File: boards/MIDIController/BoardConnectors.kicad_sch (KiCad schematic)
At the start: 5 parts, among them J2 MIDICon, J3 IO_Boards

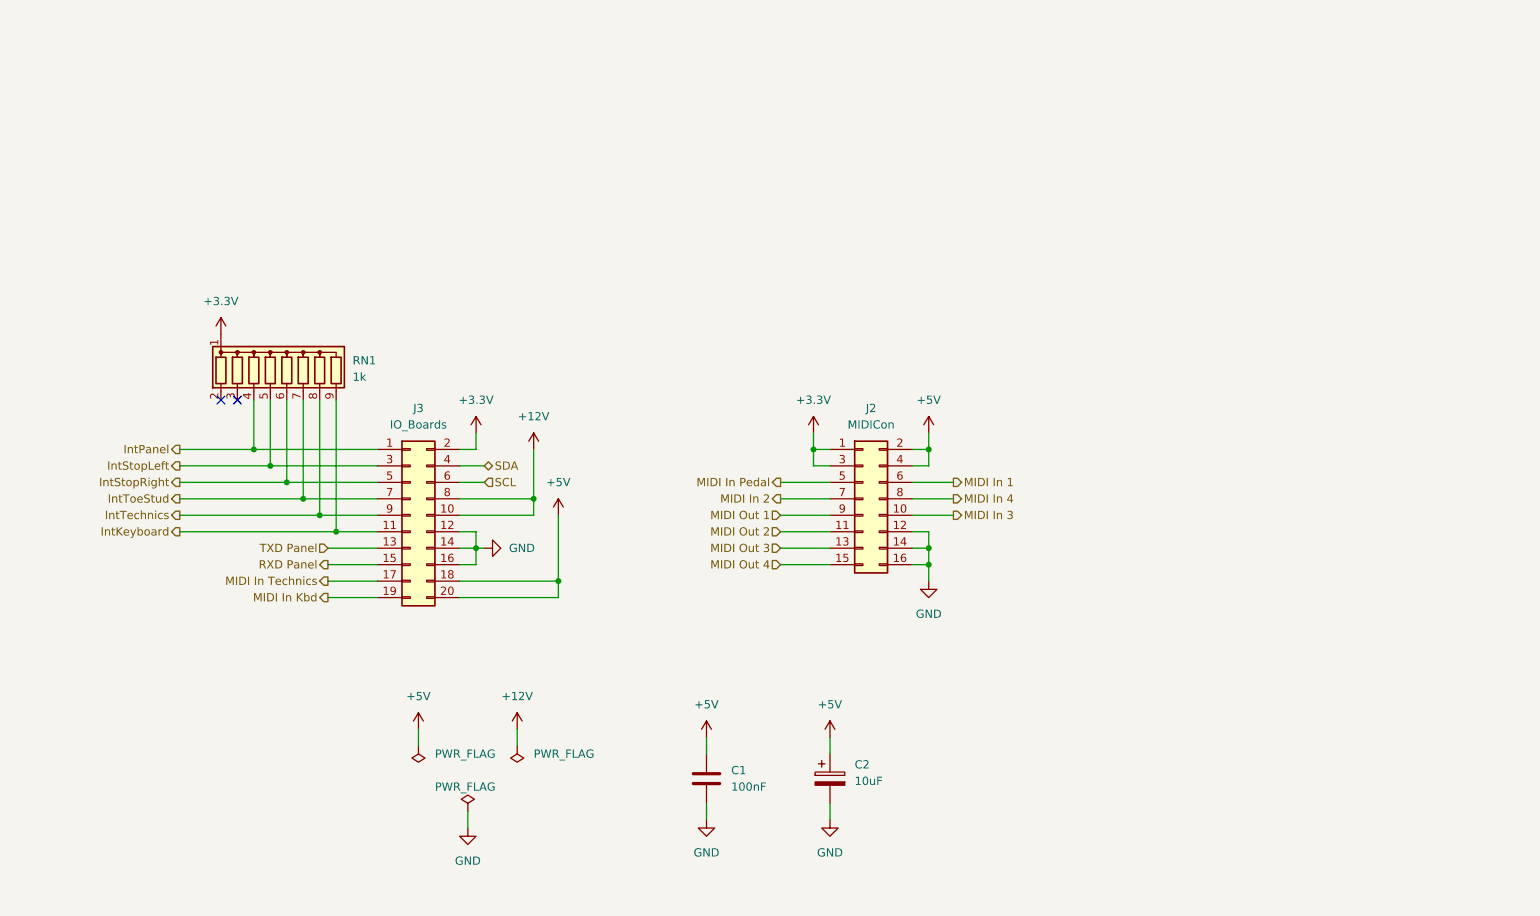
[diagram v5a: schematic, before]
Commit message: Fixed interrupt line to use open collector, added pullups to I2C lines
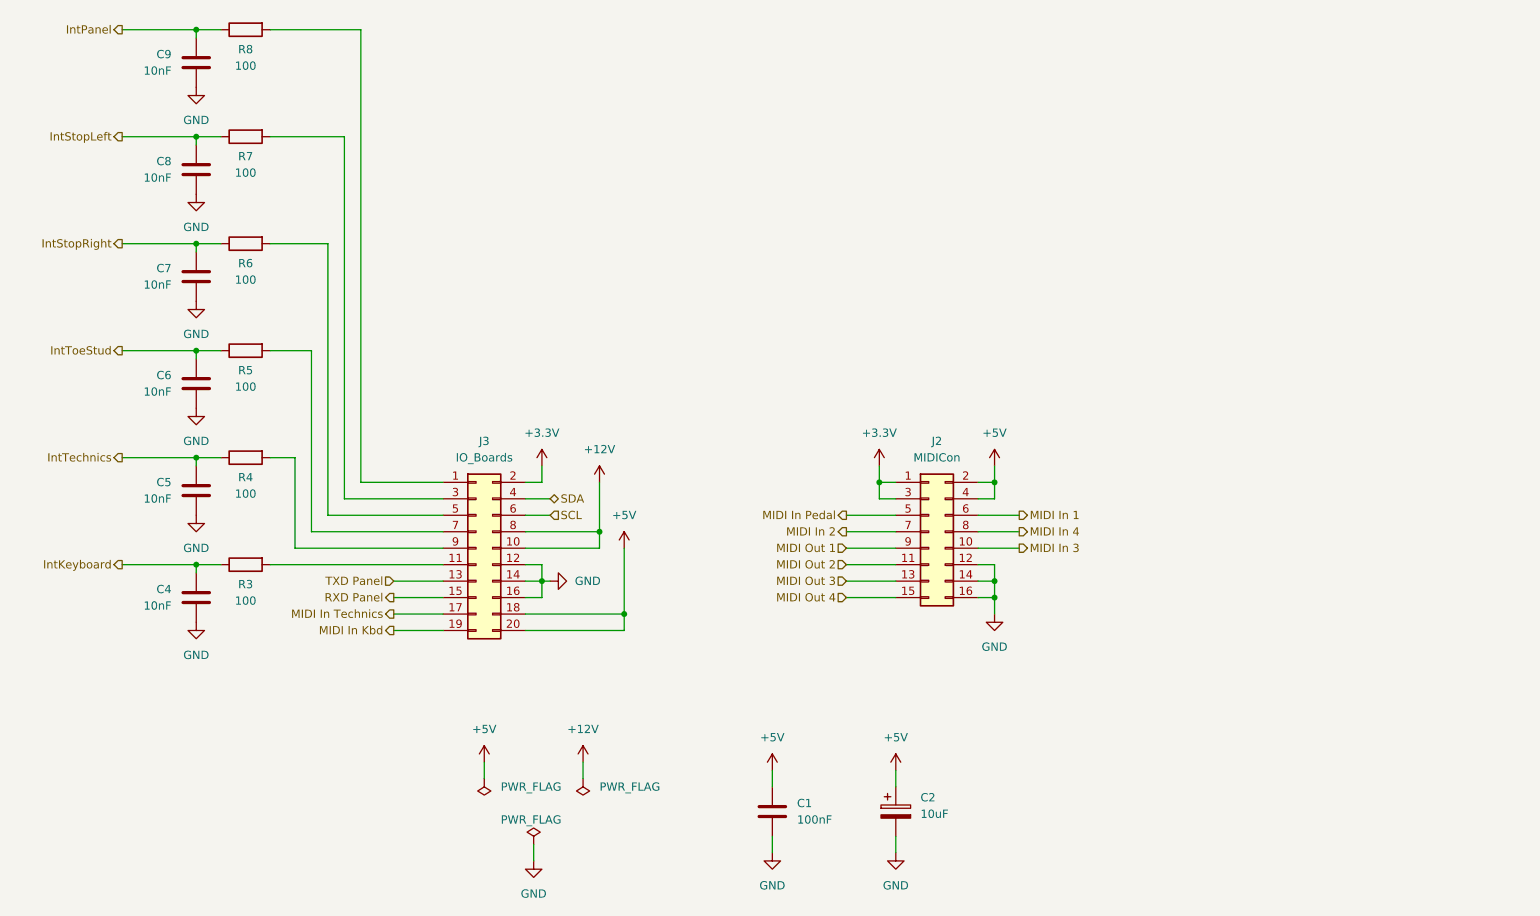
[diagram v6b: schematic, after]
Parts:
- removed RN1: 1k, Resistor_THT:R_Array_SIP9, symbol Device:R_Network08
- added C4, C5, C6, C7, C8, C9: 10nF, Capacitor_THT:C_Disc_D4.3mm_W1.9mm_P5.00mm, symbol Device:C
- added R3, R4, R5, R6, R7, R8: 100, Resistor_THT:R_Axial_DIN0207_L6.3mm_D2.5mm_P10.16mm_Horizontal, symbol Device:R
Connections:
- net GND: now also C4.2, C5.2, C6.2, C7.2, C8.2, C9.2
- net IntKeyboard: now also C4.1, R3.1; no longer J3.11 (Pin_11)
- net IntPanel: now also C9.1, R8.1; no longer J3.1 (Pin_1)
- net IntStopLeft: now also C8.1, R7.1; no longer J3.3 (Pin_3)
- net IntStopRight: now also C7.1, R6.1; no longer J3.5 (Pin_5)
- net IntTechnics: now also C5.1, R4.1; no longer J3.9 (Pin_9)
- net IntToeStud: now also C6.1, R5.1; no longer J3.7 (Pin_7)
- new net: J3.9 (Pin_9), R4.2
- new net: J3.1 (Pin_1), R8.2
- new net: J3.11 (Pin_11), R3.2
- new net: J3.3 (Pin_3), R7.2
- new net: J3.5 (Pin_5), R6.2
- new net: J3.7 (Pin_7), R5.2
- no-connect marks 2 -> 0
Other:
- moved on the sheet: C1, C2, J2, J3

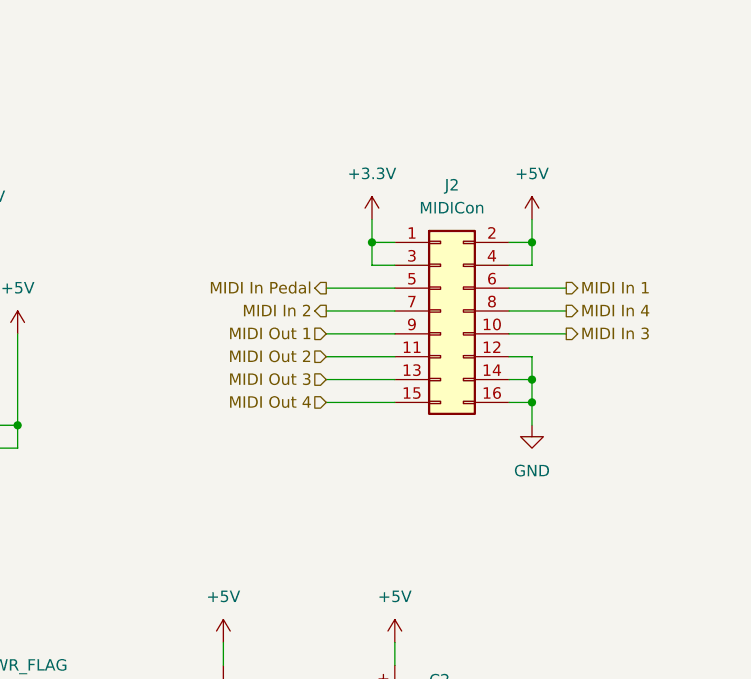
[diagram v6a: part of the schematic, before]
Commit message: Added CR2032 holder footprint, allow routing between pins
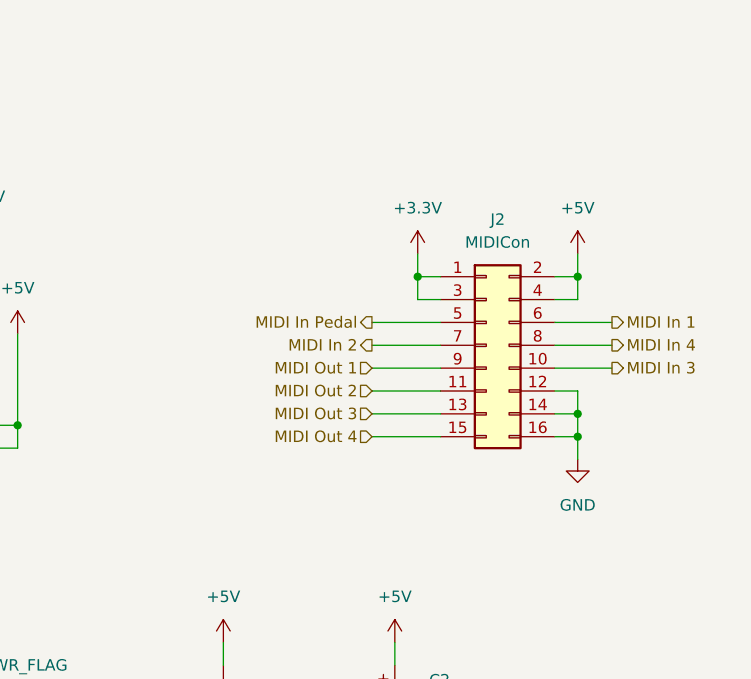
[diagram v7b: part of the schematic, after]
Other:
- moved on the sheet: J2
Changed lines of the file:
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@@
 	)
 	(junction
-		(at 181.61 111.76)
+		(at 186.69 115.57)
 		(diameter 0)
 		(color 0 0 0 0)
@@
 	)
 	(junction
-		(at 163.83 96.52)
+		(at 168.91 100.33)
 		(diameter 0)
 		(color 0 0 0 0)
 	)
 	(junction
-		(at 181.61 96.52)
+		(at 186.69 100.33)
 		(diameter 0)
 		(color 0 0 0 0)
@@
 	)
 	(junction
-		(at 181.61 114.3)
+		(at 186.69 118.11)
 		(diameter 0)
 		(color 0 0 0 0)
@@
 	(wire
 		(pts
-			(xy 179.07 104.14) (xy 185.42 104.14)
+			(xy 184.15 107.95) (xy 190.5 107.95)
 		)
 		(stroke
@@
 	(wire
 		(pts
-			(xy 181.61 114.3) (xy 181.61 116.84)
+			(xy 186.69 118.11) (xy 186.69 120.65)
 		)
 		(stroke
@@
 	(wire
 		(pts
-			(xy 163.83 99.06) (xy 166.37 99.06)
+			(xy 168.91 102.87) (xy 171.45 102.87)
 		)
 		(stroke
@@
 	(wire
 		(pts
-			(xy 179.07 114.3) (xy 181.61 114.3)
+			(xy 184.15 118.11) (xy 186.69 118.11)
 		)
 		(stroke
@@
 	(wire
 		(pts
-			(xy 179.07 99.06) (xy 181.61 99.06)
+			(xy 184.15 102.87) (xy 186.69 102.87)
 		)
 		(stroke
@@
 	(wire
 		(pts
-			(xy 181.61 96.52) (xy 181.61 93.98)
+			(xy 186.69 100.33) (xy 186.69 97.79)
 		)
 		(stroke
@@
 	(wire
 		(pts
-			(xy 163.83 96.52) (xy 166.37 96.52)
+			(xy 168.91 100.33) (xy 171.45 100.33)
 		)
 		(stroke
@@
 	(wire
 		(pts
-			(xy 181.61 109.22) (xy 181.61 111.76)
+			(xy 186.69 113.03) (xy 186.69 115.57)
 		)
 		(stroke
@@
 	(wire
 		(pts
-			(xy 179.07 101.6) (xy 185.42 101.6)
+			(xy 184.15 105.41) (xy 190.5 105.41)
 		)
 		(stroke
@@
 	(wire
 		(pts
-			(xy 158.75 114.3) (xy 166.37 114.3)
+			(xy 163.83 118.11) (xy 171.45 118.11)
 		)
 		(stroke
@@
 	(wire
 		(pts
-			(xy 158.75 101.6) (xy 166.37 101.6)
+			(xy 163.83 105.41) (xy 171.45 105.41)
 		)
 		(stroke
@@
 	(wire
 		(pts
-			(xy 179.07 111.76) (xy 181.61 111.76)
+			(xy 184.15 115.57) (xy 186.69 115.57)
 		)
 		(stroke
@@
 	(wire
 		(pts
-			(xy 163.83 96.52) (xy 163.83 99.06)
+			(xy 168.91 100.33) (xy 168.91 102.87)
 		)
 		(stroke
@@
 	(wire
 		(pts
-			(xy 179.07 106.68) (xy 185.42 106.68)
-		)
-		(stroke
-			(width 0)
-			(type default)
-		)
-	)
-	(wire
-		(pts
-			(xy 158.75 111.76) (xy 166.37 111.76)
+			(xy 184.15 110.49) (xy 190.5 110.49)
+		)
+		(stroke
+			(width 0)
+			(type default)
+		)
+	)
+	(wire
+		(pts
+			(xy 163.83 115.57) (xy 171.45 115.57)
 		)
 		(stroke
@@
 	(wire
 		(pts
-			(xy 181.61 111.76) (xy 181.61 114.3)
+			(xy 186.69 115.57) (xy 186.69 118.11)
 		)
 		(stroke
@@
 	(wire
 		(pts
-			(xy 179.07 96.52) (xy 181.61 96.52)
+			(xy 184.15 100.33) (xy 186.69 100.33)
 		)
 		(stroke
@@
 	(wire
 		(pts
-			(xy 158.75 104.14) (xy 166.37 104.14)
+			(xy 163.83 107.95) (xy 171.45 107.95)
 		)
 		(stroke
@@
 	(wire
 		(pts
-			(xy 158.75 106.68) (xy 166.37 106.68)
-		)
-		(stroke
-			(width 0)
-			(type default)
-		)
-	)
-	(wire
-		(pts
-			(xy 158.75 109.22) (xy 166.37 109.22)
-		)
-		(stroke
-			(width 0)
-			(type default)
-		)
-	)
-	(wire
-		(pts
-			(xy 163.83 93.98) (xy 163.83 96.52)
+			(xy 163.83 110.49) (xy 171.45 110.49)
+		)
+		(stroke
+			(width 0)
+			(type default)
+		)
+	)
+	(wire
+		(pts
+			(xy 163.83 113.03) (xy 171.45 113.03)
+		)
+		(stroke
+			(width 0)
+			(type default)
+		)
+	)
+	(wire
+		(pts
+			(xy 168.91 97.79) (xy 168.91 100.33)
 		)
 		(stroke
@@
 	(wire
 		(pts
-			(xy 179.07 109.22) (xy 181.61 109.22)
+			(xy 184.15 113.03) (xy 186.69 113.03)
 		)
 		(stroke
@@
 	(wire
 		(pts
-			(xy 181.61 99.06) (xy 181.61 96.52)
+			(xy 186.69 102.87) (xy 186.69 100.33)
 		)
 		(stroke
@@
 	(hierarchical_label "MIDI Out 4"
 		(shape input)
-		(at 158.75 114.3 180)
+		(at 163.83 118.11 180)
 		(fields_autoplaced yes)
 		(effects
@@
 	(hierarchical_label "MIDI Out 1"
 		(shape input)
-		(at 158.75 106.68 180)
+		(at 163.83 110.49 180)
 		(fields_autoplaced yes)
 		(effects
@@
 	(hierarchical_label "MIDI In 4"
 		(shape output)
-		(at 185.42 104.14 0)
+		(at 190.5 107.95 0)
 		(fields_autoplaced yes)
 		(effects
@@
 	(hierarchical_label "MIDI Out 2"
 		(shape input)
-		(at 158.75 109.22 180)
+		(at 163.83 113.03 180)
 		(fields_autoplaced yes)
 		(effects
@@
 	(hierarchical_label "MIDI Out 3"
 		(shape input)
-		(at 158.75 111.76 180)
+		(at 163.83 115.57 180)
 		(fields_autoplaced yes)
 		(effects
@@
 	(hierarchical_label "MIDI In 3"
 		(shape output)
-		(at 185.42 106.68 0)
+		(at 190.5 110.49 0)
 		(fields_autoplaced yes)
 		(effects
@@
 	(hierarchical_label "MIDI In Pedal"
 		(shape output)
-		(at 158.75 101.6 180)
+		(at 163.83 105.41 180)
 		(fields_autoplaced yes)
 		(effects
@@
 	(hierarchical_label "MIDI In 2"
 		(shape output)
-		(at 158.75 104.14 180)
+		(at 163.83 107.95 180)
 		(fields_autoplaced yes)
 		(effects
@@
 	(hierarchical_label "MIDI In 1"
 		(shape output)
-		(at 185.42 101.6 0)
+		(at 190.5 105.41 0)
 		(fields_autoplaced yes)
 		(effects
@@
 	(symbol
 		(lib_id "power:+3.3V")
-		(at 163.83 93.98 0)
+		(at 168.91 97.79 0)
 		(unit 1)
 		(exclude_from_sim no)
@@
 		(fields_autoplaced yes)
 		(property "Reference" "#PWR03"
-			(at 163.83 97.79 0)
+			(at 168.91 101.6 0)
 			(effects
 				(font
@@
 		)
 		(property "Value" "+3.3V"
-			(at 163.83 88.9 0)
+			(at 168.91 92.71 0)
 			(effects
 				(font
@@
 		)
 		(property "Footprint" ""
-			(at 163.83 93.98 0)
+			(at 168.91 97.79 0)
 			(effects
 				(font
@@
 		)
 		(property "Datasheet" ""
-			(at 163.83 93.98 0)
+			(at 168.91 97.79 0)
 			(effects
 				(font
@@
 		)
 		(property "Description" "Power symbol creates a global label with name \"+3.3V\""
-			(at 163.83 93.98 0)
+			(at 168.91 97.79 0)
 			(effects
 				(font
@@
 	(symbol
 		(lib_id "Connector_Generic:Conn_02x08_Odd_Even")
-		(at 171.45 104.14 0)
+		(at 176.53 107.95 0)
 		(unit 1)
 		(exclude_from_sim no)
@@
 		(fields_autoplaced yes)
 		(property "Reference" "J2"
-			(at 172.72 90.17 0)
+			(at 177.8 93.98 0)
 			(effects
 				(font
@@
 		)
 		(property "Value" "MIDICon"
-			(at 172.72 92.71 0)
+			(at 177.8 96.52 0)
 			(effects
 				(font
@@
 		)
 		(property "Footprint" "Connector_IDC:IDC-Header_2x08_P2.54mm_Vertical"
-			(at 171.45 104.14 0)
+			(at 176.53 107.95 0)
 			(effects
 				(font
@@
 		)
 		(property "Datasheet" "~"
-			(at 171.45 104.14 0)
+			(at 176.53 107.95 0)
 			(effects
 				(font
@@
 		)
 		(property "Description" "Generic connector, double row, 02x08, odd/even pin numbering scheme (row 1 odd numbers, row 2 even numbers), script generated (kicad-library-utils/schlib/autogen/connector/)"
-			(at 171.45 104.14 0)
+			(at 176.53 107.95 0)
 			(effects
 				(font
@@
 	(symbol
 		(lib_id "power:GND")
-		(at 181.61 116.84 0)
+		(at 186.69 120.65 0)
 		(unit 1)
 		(exclude_from_sim no)
@@
 		(fields_autoplaced yes)
 		(property "Reference" "#PWR02"
-			(at 181.61 123.19 0)
+			(at 186.69 127 0)
 			(effects
 				(font
@@
 		)
 		(property "Value" "GND"
-			(at 181.61 121.92 0)
+			(at 186.69 125.73 0)
 			(effects
 				(font
@@
 		)
 		(property "Footprint" ""
-			(at 181.61 116.84 0)
+			(at 186.69 120.65 0)
 			(effects
 				(font
@@
 		)
 		(property "Datasheet" ""
-			(at 181.61 116.84 0)
+			(at 186.69 120.65 0)
 			(effects
 				(font
@@
 		)
 		(property "Description" "Power symbol creates a global label with name \"GND\" , ground"
-			(at 181.61 116.84 0)
+			(at 186.69 120.65 0)
 			(effects
 				(font
@@
 	(symbol
 		(lib_id "power:+5V")
-		(at 181.61 93.98 0)
+		(at 186.69 97.79 0)
 		(unit 1)
 		(exclude_from_sim no)
@@
 		(fields_autoplaced yes)
 		(property "Reference" "#PWR01"
-			(at 181.61 97.79 0)
+			(at 186.69 101.6 0)
 			(effects
 				(font
@@
 		)
 		(property "Value" "+5V"
-			(at 181.61 88.9 0)
+			(at 186.69 92.71 0)
 			(effects
 				(font
@@
 		)
 		(property "Footprint" ""
-			(at 181.61 93.98 0)
+			(at 186.69 97.79 0)
 			(effects
 				(font
@@
 		)
 		(property "Datasheet" ""
-			(at 181.61 93.98 0)
+			(at 186.69 97.79 0)
 			(effects
 				(font
@@
 		)
 		(property "Description" "Power symbol creates a global label with name \"+5V\""
-			(at 181.61 93.98 0)
-			(effects
-				(font
+			(at 186.69 97.79 0)
+			(effects
+				(font
